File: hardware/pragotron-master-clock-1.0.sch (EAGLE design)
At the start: 64 parts, among them IC1 ATSAMD21E18A-MU, IC2 AP2112K-3.3, IC3 MIC2288YD5-TR, IC4 DS3231MZ+, J1 USB-C, J2 TRMBLK_3.5MM_2P, J3 2X5_PITCH_1.27MMTH_NOKEY_UNSH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, Q1 N-MOSFET, Q2 N-MOSFET, Q3 N-MOSFET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

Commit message: board layout
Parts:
- S1: value TSA063G60-250 -> SKRPACE010; device BASTL_SWITCHES:PUSH_MOMENTARY_SMT_6X6MM_SMALL_PADS -> BASTL_SWITCHES:SKRPACE010
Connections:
- net !RESET: now also S1.3, S1.4; no longer S1.1
- net 32KHZ: now also IC1.PA07; no longer IC1.PA06
- net A: now also IC1.PA00; no longer IC1.PA16
- net B: now also IC1.PA01; no longer IC1.PA17
- net BOOST_EN: now also IC1.PA09
- net C: now also IC1.PA02; no longer IC1.PA18
- net D: now also IC1.PA03; no longer IC1.PA19
- net FAST/LEFT: now also IC1.PA16; no longer IC1.PA00
- net GND: now also S1.1
- net INT/SQW: now also IC1.PA06; no longer IC1.PA07
- net MINUTE/OK: now also IC1.PA18; no longer IC1.PA02
- net XFAST/RIGHT: now also IC1.PA17; no longer IC1.PA01
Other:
- moved on the sheet: J4

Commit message: finish board, add gerber, bom and cpl
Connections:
- removed net +3.3V: C12.1, C13.1, C14.1, C3.1, C4.1, IC1.VDDANA, IC1.VDDIN, IC2.VOUT, IC4.VCC, J4.2, R16.2, R17.2
- net VDD: now also C12.1, C13.1, C14.1, C3.1, C4.1, IC1.VDDANA, IC1.VDDIN, IC2.VOUT, IC4.VCC, J4.2, R16.2, R17.2

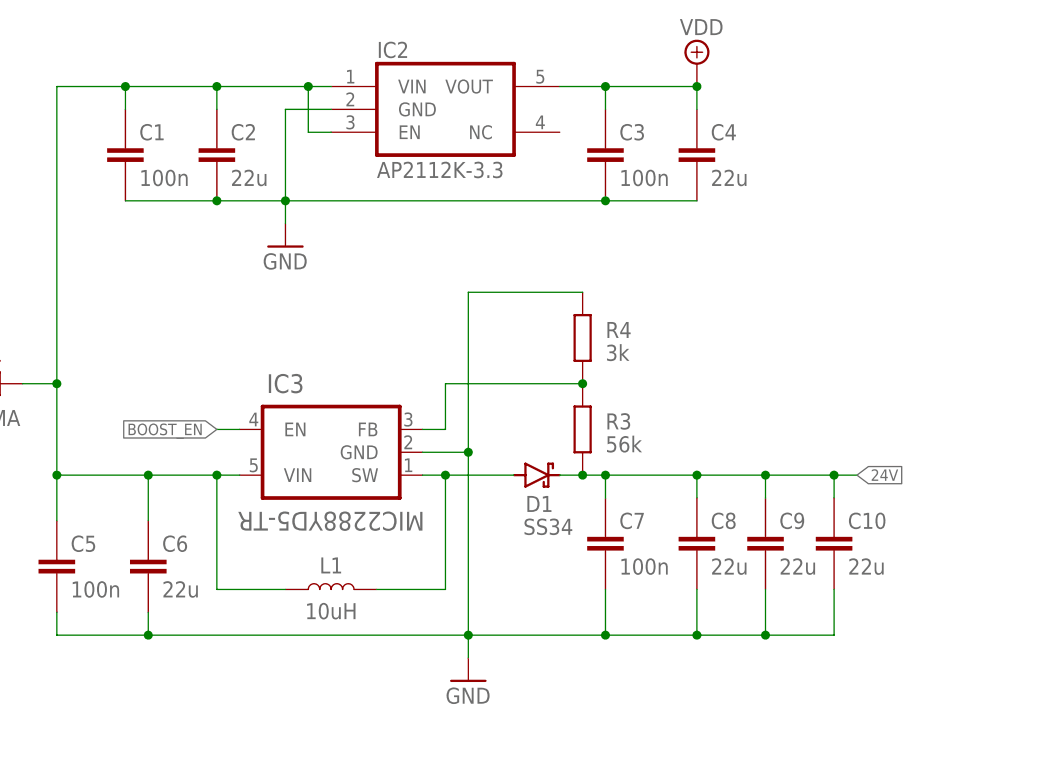
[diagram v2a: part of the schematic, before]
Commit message: replace 22u with 10u caps (there are no 50V caps in 22u)
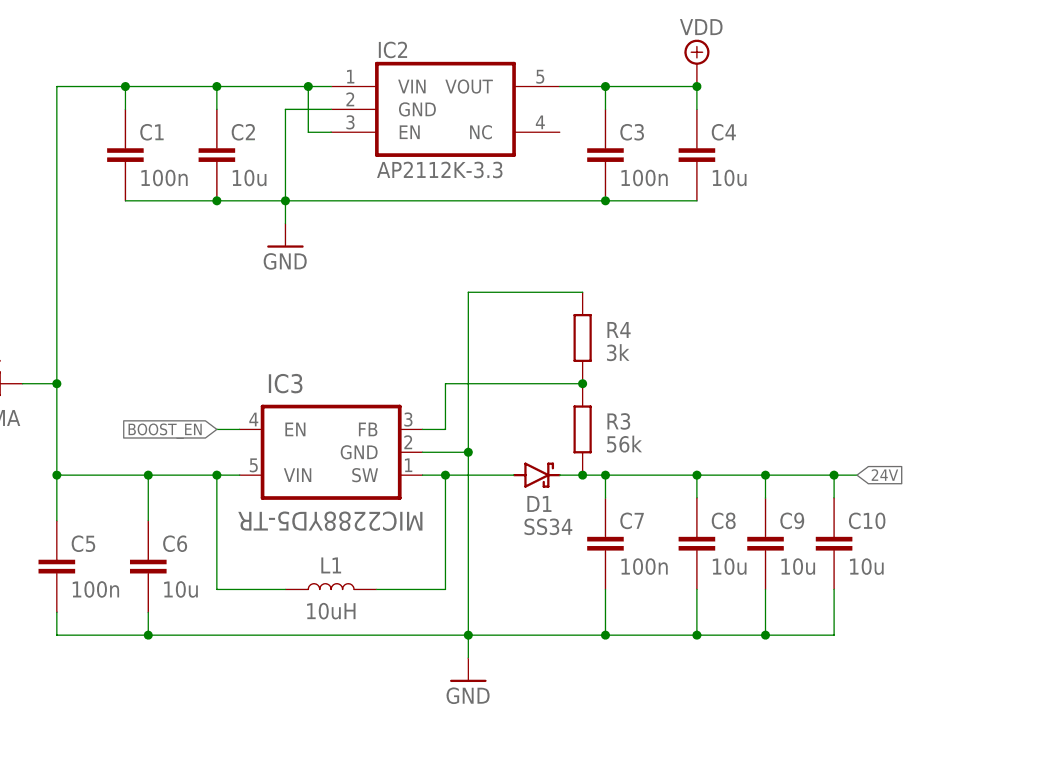
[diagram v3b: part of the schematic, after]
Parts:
- C10, C2, C4, C6, C8, C9: value 22u -> 10u
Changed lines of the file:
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@@
 <part name="GND2" library="BASTL_SYMBOLS" library_urn="urn:adsk.eagle:library:32975873" deviceset="GND" device=""/>
 <part name="C1" library="BASTL_CAPACITORS" library_urn="urn:adsk.eagle:library:32978038" deviceset="CAPACITOR0603" device="" package3d_urn="urn:adsk.eagle:package:32978072/2" value="100n"/>
-<part name="C2" library="BASTL_CAPACITORS" library_urn="urn:adsk.eagle:library:32978038" deviceset="CAPACITOR0805" device="" package3d_urn="urn:adsk.eagle:package:32978071/3" value="22u"/>
+<part name="C2" library="BASTL_CAPACITORS" library_urn="urn:adsk.eagle:library:32978038" deviceset="CAPACITOR0805" device="" package3d_urn="urn:adsk.eagle:package:32978071/3" value="10u"/>
 <part name="C3" library="BASTL_CAPACITORS" library_urn="urn:adsk.eagle:library:32978038" deviceset="CAPACITOR0603" device="" package3d_urn="urn:adsk.eagle:package:32978072/2" value="100n"/>
-<part name="C4" library="BASTL_CAPACITORS" library_urn="urn:adsk.eagle:library:32978038" deviceset="CAPACITOR0805" device="" package3d_urn="urn:adsk.eagle:package:32978071/3" value="22u"/>
+<part name="C4" library="BASTL_CAPACITORS" library_urn="urn:adsk.eagle:library:32978038" deviceset="CAPACITOR0805" device="" package3d_urn="urn:adsk.eagle:package:32978071/3" value="10u"/>
 <part name="C5" library="BASTL_CAPACITORS" library_urn="urn:adsk.eagle:library:32978038" deviceset="CAPACITOR0603" device="" package3d_urn="urn:adsk.eagle:package:32978072/2" value="100n"/>
-<part name="C6" library="BASTL_CAPACITORS" library_urn="urn:adsk.eagle:library:32978038" deviceset="CAPACITOR0805" device="" package3d_urn="urn:adsk.eagle:package:32978071/3" value="22u"/>
+<part name="C6" library="BASTL_CAPACITORS" library_urn="urn:adsk.eagle:library:32978038" deviceset="CAPACITOR0805" device="" package3d_urn="urn:adsk.eagle:package:32978071/3" value="10u"/>
 <part name="C7" library="BASTL_CAPACITORS" library_urn="urn:adsk.eagle:library:32978038" deviceset="CAPACITOR0603" device="" package3d_urn="urn:adsk.eagle:package:32978072/2" value="100n"/>
-<part name="C8" library="BASTL_CAPACITORS" library_urn="urn:adsk.eagle:library:32978038" deviceset="CAPACITOR0805" device="" package3d_urn="urn:adsk.eagle:package:32978071/3" value="22u"/>
+<part name="C8" library="BASTL_CAPACITORS" library_urn="urn:adsk.eagle:library:32978038" deviceset="CAPACITOR0805" device="" package3d_urn="urn:adsk.eagle:package:32978071/3" value="10u"/>
 <part name="GND3" library="BASTL_SYMBOLS" library_urn="urn:adsk.eagle:library:32975873" deviceset="GND" device=""/>
-<part name="C9" library="BASTL_CAPACITORS" library_urn="urn:adsk.eagle:library:32978038" deviceset="CAPACITOR0805" device="" package3d_urn="urn:adsk.eagle:package:32978071/3" value="22u"/>
-<part name="C10" library="BASTL_CAPACITORS" library_urn="urn:adsk.eagle:library:32978038" deviceset="CAPACITOR0805" device="" package3d_urn="urn:adsk.eagle:package:32978071/3" value="22u"/>
+<part name="C9" library="BASTL_CAPACITORS" library_urn="urn:adsk.eagle:library:32978038" deviceset="CAPACITOR0805" device="" package3d_urn="urn:adsk.eagle:package:32978071/3" value="10u"/>
+<part name="C10" library="BASTL_CAPACITORS" library_urn="urn:adsk.eagle:library:32978038" deviceset="CAPACITOR0805" device="" package3d_urn="urn:adsk.eagle:package:32978071/3" value="10u"/>
 <part name="R5" library="BASTL_RESISTORS" library_urn="urn:adsk.eagle:library:32975925" deviceset="RESISTOR0603" device="" package3d_urn="urn:adsk.eagle:package:32975936/2" value="10k"/>
 <part name="R6" library="BASTL_RESISTORS" library_urn="urn:adsk.eagle:library:32975925" deviceset="RESISTOR0603" device="" package3d_urn="urn:adsk.eagle:package:32975936/2" value="10k"/>

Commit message: add schematic notes, remove old bom/cpl
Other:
- note added: "N-MOSFET types: BSH103,215 AO3400A"
- note added: "P-MOSFET types: BSS84-7-F"
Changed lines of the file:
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@@
 <text x="-73.66" y="-55.88" size="10.16" layer="98" ratio="10">H-BRIDGE &amp; OUTPUT</text>
 <text x="228.6" y="45.72" size="10.16" layer="98" ratio="10">RTC</text>
+<text x="-10.16" y="-132.08" size="1.778" layer="98">P-MOSFET types:
+BSS84-7-F</text>
+<text x="25.4" y="-134.62" size="1.778" layer="98">N-MOSFET types:
+BSH103,215
+AO3400A</text>
 </plain>
 <instances>
@@
 </drawing>
 <compatibility>
+<note version="6.3" minversion="6.2.2" severity="warning">
+Since Version 6.2.2 text objects can contain more than one line,
+which will not be processed correctly with this version.
+</note>
 <note version="8.2" severity="warning">
 Since Version 8.2, EAGLE supports online libraries. The ids
